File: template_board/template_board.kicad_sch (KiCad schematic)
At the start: 3 parts

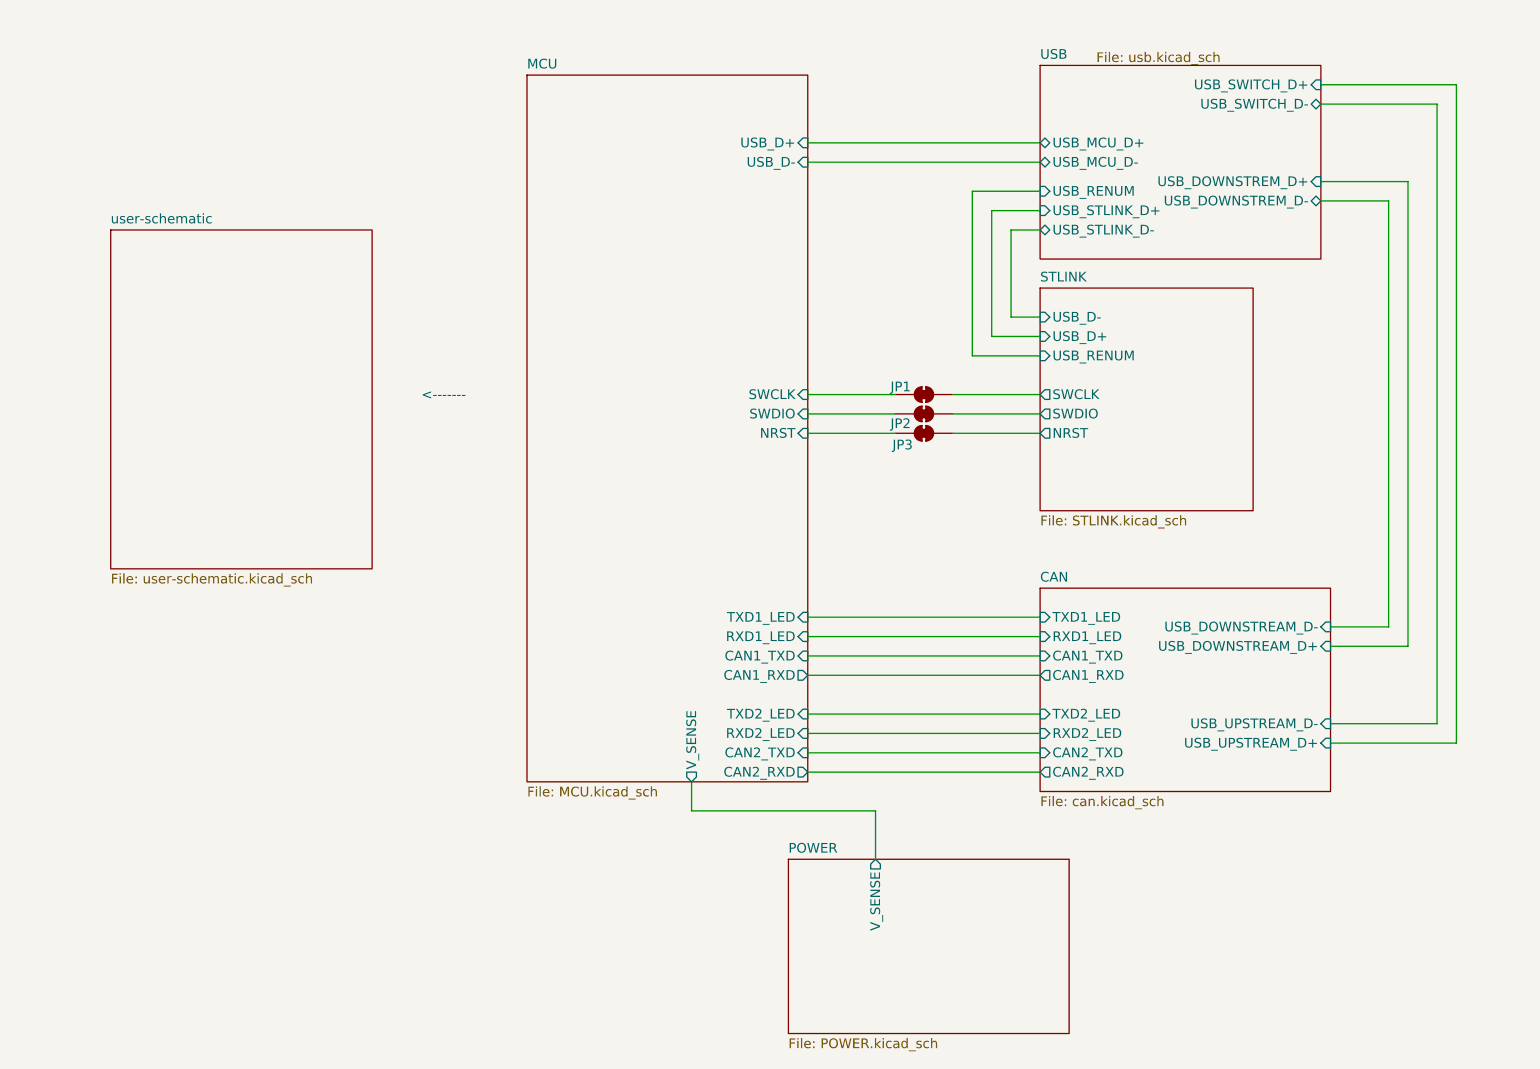
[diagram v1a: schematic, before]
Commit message: updated all subschematics
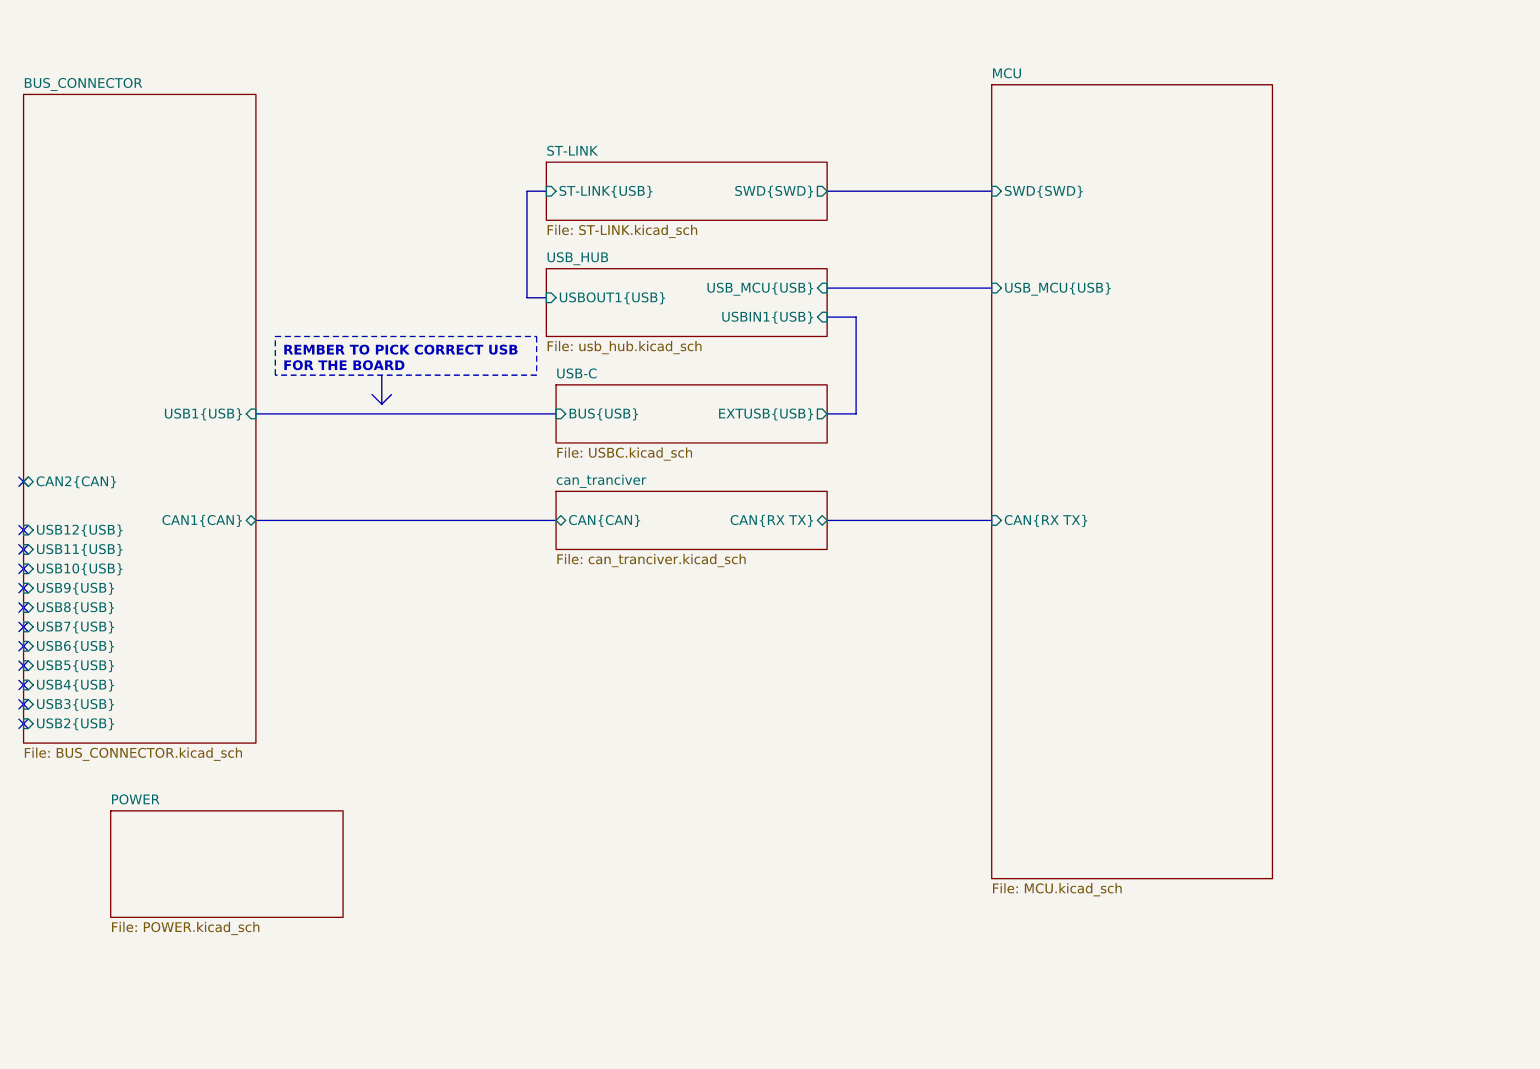
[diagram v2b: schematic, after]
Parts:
- removed JP1, JP2, JP3: SolderJumper_2_Bridged, Jumper:SolderJumper-2_P1.3mm_Open_RoundedPad1.0x1.5mm, symbol Jumper:SolderJumper_2_Bridged
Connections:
- no-connect marks 0 -> 12
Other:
- removed sheet CAN
- removed sheet STLINK
- removed sheet USB
- removed sheet user-schematic
- added sheet BUS_CONNECTOR (BUS_CONNECTOR.kicad_sch)
- added sheet ST-LINK (ST-LINK.kicad_sch)
- added sheet USB-C (USBC.kicad_sch)
- added sheet USB_HUB (usb_hub.kicad_sch)
- added sheet can_tranciver (can_tranciver.kicad_sch)
- sheet MCU ports: added CAN{RX TX}, SWD{SWD}, USB_MCU{USB}; removed CAN1_RXD, CAN1_TXD, CAN2_RXD, CAN2_TXD, NRST, RXD1_LED, RXD2_LED, SWCLK, SWDIO, TXD1_LED, TXD2_LED, USB_D+, USB_D-, V_SENSE
- sheet POWER ports: added none; removed V_SENSE
- note removed: "<-------"

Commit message: can transiver update
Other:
- sheet POWER ports: added POWER_EN; removed none
- sheet can_tranciver ports: added POWER_EN; removed none
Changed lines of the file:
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@@
 		(members "D+" "D-")
 	)
+	(junction
+		(at 57.404 134.62)
+		(diameter 0)
+		(color 0 0 0 0)
+	)
 	(no_connect
 		(at 27.94 92.71)
@@
 		)
 	)
+	(wire
+		(pts
+			(xy 57.404 134.62) (xy 76.2 134.62)
+		)
+		(stroke
+			(width 0)
+			(type default)
+		)
+	)
 	(bus
 		(pts
@@
 		)
 	)
+	(wire
+		(pts
+			(xy 57.15 134.62) (xy 57.404 134.62)
+		)
+		(stroke
+			(width 0)
+			(type default)
+		)
+	)
 	(polyline
 		(pts
@@
 		)
 	)
+	(wire
+		(pts
+			(xy 76.2 134.62) (xy 76.2 95.25)
+		)
+		(stroke
+			(width 0)
+			(type default)
+		)
+	)
 	(bus
 		(pts
 			(xy 58.42 91.44) (xy 97.79 91.44)
+		)
+		(stroke
+			(width 0)
+			(type default)
+		)
+	)
+	(wire
+		(pts
+			(xy 76.2 95.25) (xy 97.79 95.25)
 		)
 		(stroke
@@
 	(sheet
 		(at 97.79 87.63)
-		(size 35.56 7.62)
+		(size 35.56 10.668)
 		(fields_autoplaced yes)
 		(stroke
@@
 		)
 		(property "Sheetfile" "can_tranciver.kicad_sch"
-			(at 97.79 95.8346 0)
+			(at 97.79 98.8826 0)
 			(effects
 				(font
@@
 		(pin "CAN{CAN}" bidirectional
 			(at 97.79 91.44 180)
+			(effects
+				(font
+					(size 1.27 1.27)
+				)
+				(justify left)
+			)
+		)
+		(pin "POWER_EN" output
+			(at 97.79 95.25 180)
 			(effects
 				(font
@@
 	)
 	(sheet
-		(at 39.37 129.54)
+		(at 26.924 130.048)
 		(size 30.48 13.97)
 		(fields_autoplaced yes)
@@
 		)
 		(property "Sheetname" "POWER"
-			(at 39.37 128.8284 0)
+			(at 26.924 129.3364 0)
 			(effects
 				(font
@@
 		)
 		(property "Sheetfile" "POWER.kicad_sch"
-			(at 39.37 144.0946 0)
+			(at 26.924 144.6026 0)
 			(effects
 				(font
@@
 			)
 		)
+		(pin "POWER_EN" input
+			(at 57.404 134.62 0)
+			(effects
+				(font
+					(size 1.27 1.27)
+				)
+				(justify right)
+			)
+		)

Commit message: chamt skończony chyba
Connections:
- no-connect marks 12 -> 15
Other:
- sheet BUS_CONNECTOR ports: added CAN3{CAN}, CAN4{CAN}, GPIO[0..35]; removed none
- sheet MCU ports: added CAN_TRANSIVER{SPI}; removed none
- sheet can_tranciver ports: added CAN_TRANSIVER{SPI}; removed none

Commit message: schemat skończony
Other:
- sheet MCU ports: added STLINK_UART{UART}; removed none
- sheet ST-LINK ports: added STLINK_UART{UART}; removed none
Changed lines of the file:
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@@
+	(bus
+		(pts
+			(xy 166.37 52.07) (xy 187.96 52.07)
+		)
+		(stroke
+			(width 0)
+			(type default)
+		)
+	)
 	(bus
 		(pts
@@
 	(bus
 		(pts
-			(xy 127 53.34) (xy 129.54 53.34)
-		)
-		(stroke
-			(width 0)
-			(type default)
-		)
-	)
-	(bus
-		(pts
-			(xy 166.37 53.34) (xy 187.96 53.34)
+			(xy 127 52.07) (xy 129.54 52.07)
+		)
+		(stroke
+			(width 0)
+			(type default)
+		)
+	)
+	(bus
+		(pts
+			(xy 166.37 49.53) (xy 187.96 49.53)
 		)
 		(stroke
@@
 	(bus
 		(pts
-			(xy 127 67.31) (xy 127 53.34)
+			(xy 127 67.31) (xy 127 52.07)
 		)
 		(stroke
@@
 	(text_box "REMBER \nTO \nPICK \nCORRECT \nUSB \nFOR \nTHE BOARD"
 		(exclude_from_sim no)
-		(at 45.085 95.25 0)
+		(at 45.085 94.615 0)
 		(size 30.48 30.48)
 		(stroke
@@
 			)
 		)
-		(pin "SWD{SWD}" input
-			(at 187.96 53.34 180)
-			(effects
-				(font
-					(size 1.27 1.27)
-				)
-				(justify left)
-			)
-		)
 		(pin "USB_MCU{USB}" input
 			(at 187.96 66.04 180)
@@
 		(pin "CAN_TRANSIVER{SPI}" bidirectional
 			(at 187.96 106.68 180)
+			(effects
+				(font
+					(size 1.27 1.27)
+				)
+				(justify left)
+			)
+		)
+		(pin "STLINK_UART{UART}" bidirectional
+			(at 187.96 52.07 180)
+			(effects
+				(font
+					(size 1.27 1.27)
+				)
+				(justify left)
+			)
+		)
+		(pin "SWD{SWD}" input
+			(at 187.96 49.53 180)
 			(effects
 				(font
@@
 	)
 	(sheet
-		(at 129.54 49.53)
-		(size 36.83 7.62)
+		(at 129.54 46.99)
+		(size 36.83 10.16)
 		(fields_autoplaced yes)
 		(stroke
@@
 		)
 		(property "Sheetname" "ST-LINK"
-			(at 129.54 48.8184 0)
+			(at 129.54 46.2784 0)
 			(effects
 				(font
@@
 			)
 		)
+		(pin "STLINK_UART{UART}" bidirectional
+			(at 166.37 52.07 0)
+			(effects
+				(font
+					(size 1.27 1.27)
+				)
+				(justify right)
+			)
+		)
+		(pin "SWD{SWD}" output
+			(at 166.37 49.53 0)
+			(effects
+				(font
+					(size 1.27 1.27)
+				)
+				(justify right)
+			)
+		)
 		(pin "ST-LINK{USB}" input
-			(at 129.54 53.34 180)
-			(effects
-				(font
-					(size 1.27 1.27)
-				)
-				(justify left)
-			)
-		)
-		(pin "SWD{SWD}" output
-			(at 166.37 53.34 0)
-			(effects
-				(font
-					(size 1.27 1.27)
-				)
-				(justify right)
-			)
-		)
+			(at 129.54 52.07 180)
+			(effects
+				(font
+					(size 1.27 1.27)
+				)
+				(justify left)
+			)
+		)

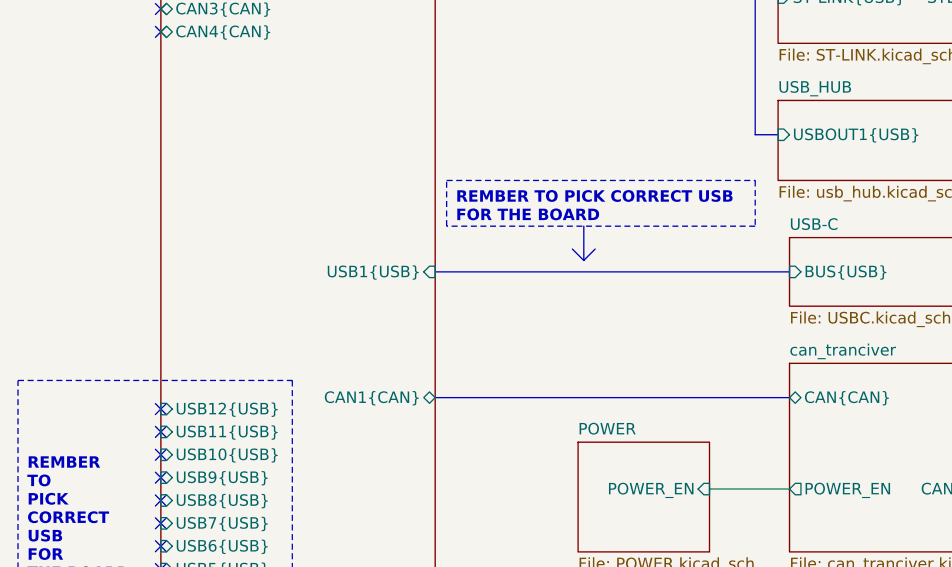
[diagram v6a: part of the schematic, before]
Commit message: [schematics] fixed issue with: stlink->crystal capacitors, usb-> esd with too big capacitance, tranzistor for stlink-usb renum changed
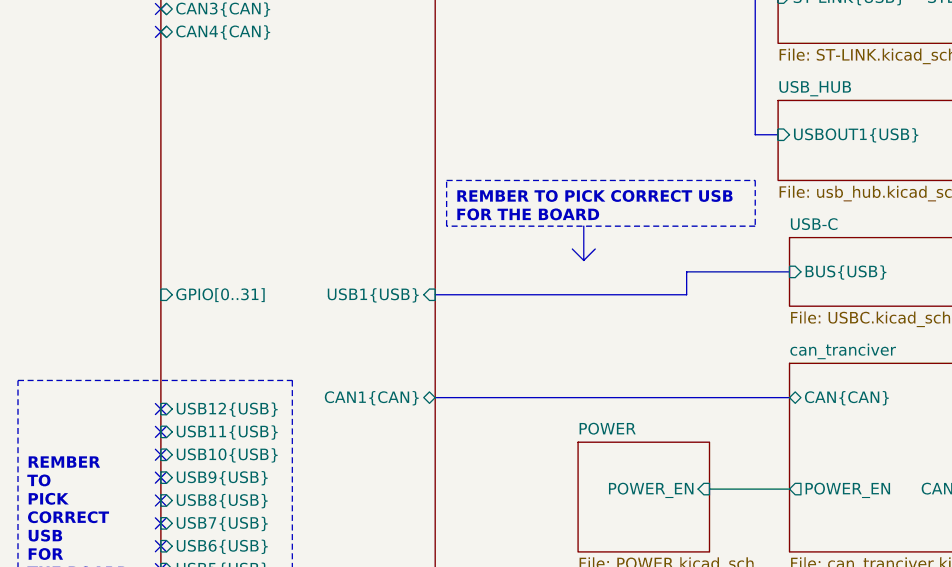
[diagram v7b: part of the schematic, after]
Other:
- sheet BUS_CONNECTOR ports: added GPIO[0..31]; removed none
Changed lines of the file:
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@@
+		)
+	)
+	(bus
+		(pts
+			(xy 119.38 82.55) (xy 130.81 82.55)
+		)
+		(stroke
+			(width 0)
+			(type default)
 		)
 	)
@@
 		)
 	)
+	(bus
+		(pts
+			(xy 91.44 85.09) (xy 119.38 85.09)
+		)
+		(stroke
+			(width 0)
+			(type default)
+		)
+	)
 	(polyline
 		(pts
@@
 	(bus
 		(pts
-			(xy 91.44 82.55) (xy 130.81 82.55)
+			(xy 119.38 85.09) (xy 119.38 82.55)
 		)
 		(stroke
@@
 			)
 		)
-		(pin "USB1{USB}" input
-			(at 91.44 82.55 0)
-			(effects
-				(font
-					(size 1.27 1.27)
-				)
-				(justify right)
-			)
-		)
 		(pin "USB2{USB}" input
 			(at 60.96 123.19 180)
@@
 				)
 				(justify right)
+			)
+		)
+		(pin "USB1{USB}" input
+			(at 91.44 85.09 0)
+			(effects
+				(font
+					(size 1.27 1.27)
+				)
+				(justify right)
+			)
+		)
+		(pin "GPIO[0..31]" input
+			(at 60.96 85.09 180)
+			(effects
+				(font
+					(size 1.27 1.27)
+				)
+				(justify left)
 			)
 		)
@@
 			)
 		)
+		(pin "EXTUSB{USB}" output
+			(at 166.37 82.55 0)
+			(effects
+				(font
+					(size 1.27 1.27)
+				)
+				(justify right)
+			)
+		)
 		(pin "BUS{USB}" input
 			(at 130.81 82.55 180)
@@
 			)
 		)
-		(pin "EXTUSB{USB}" output
-			(at 166.37 82.55 0)
-			(effects
-				(font
-					(size 1.27 1.27)
-				)
-				(justify right)
-			)
-		)

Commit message: [schematics] complete lora board
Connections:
- no-connect marks 15 -> 14
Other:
- added sheet LORA (lora.kicad_sch)
- sheet BUS_CONNECTOR ports: added none; removed GPIO[0..35]
- sheet MCU ports: added GPIO[0..31], LORA_DIO[0..5], LORA{SPI}, ~{LORA_RESET}; removed none
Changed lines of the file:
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@@
 		(at 60.96 50.8)
 	)
-	(no_connect
-		(at 91.44 50.8)
+	(bus
+		(pts
+			(xy 166.37 49.53) (xy 187.96 49.53)
+		)
+		(stroke
+			(width 0)
+			(type default)
+		)
+	)
+	(bus
+		(pts
+			(xy 119.38 82.55) (xy 130.81 82.55)
+		)
+		(stroke
+			(width 0)
+			(type default)
+		)
+	)
+	(polyline
+		(pts
+			(xy 106.68 80.01) (xy 107.95 81.28)
+		)
+		(stroke
+			(width 0)
+			(type default)
+		)
+	)
+	(bus
+		(pts
+			(xy 166.37 33.02) (xy 187.96 33.02)
+		)
+		(stroke
+			(width 0)
+			(type default)
+		)
+	)
+	(wire
+		(pts
+			(xy 121.92 106.68) (xy 130.81 106.68)
+		)
+		(stroke
+			(width 0)
+			(type default)
+		)
+	)
+	(bus
+		(pts
+			(xy 171.45 69.85) (xy 166.37 69.85)
+		)
+		(stroke
+			(width 0)
+			(type default)
+		)
+	)
+	(bus
+		(pts
+			(xy 127 52.07) (xy 129.54 52.07)
+		)
+		(stroke
+			(width 0)
+			(type default)
+		)
+	)
+	(bus
+		(pts
+			(xy 91.44 85.09) (xy 119.38 85.09)
+		)
+		(stroke
+			(width 0)
+			(type default)
+		)
+	)
+	(polyline
+		(pts
+			(xy 107.95 81.28) (xy 109.22 80.01)
+		)
+		(stroke
+			(width 0)
+			(type default)
+		)
+	)
+	(wire
+		(pts
+			(xy 166.37 35.56) (xy 187.96 35.56)
+		)
+		(stroke
+			(width 0)
+			(type default)
+		)
 	)
 	(bus
@@
 	(bus
 		(pts
-			(xy 119.38 82.55) (xy 130.81 82.55)
+			(xy 166.37 66.04) (xy 187.96 66.04)
+		)
+		(stroke
+			(width 0)
+			(type default)
+		)
+	)
+	(bus
+		(pts
+			(xy 166.37 96.52) (xy 187.96 96.52)
 		)
 		(stroke
@@
 	(polyline
 		(pts
-			(xy 106.68 80.01) (xy 107.95 81.28)
-		)
-		(stroke
-			(width 0)
-			(type default)
-		)
-	)
-	(wire
-		(pts
-			(xy 121.92 106.68) (xy 130.81 106.68)
-		)
-		(stroke
-			(width 0)
-			(type default)
-		)
-	)
-	(bus
-		(pts
-			(xy 166.37 66.04) (xy 187.96 66.04)
+			(xy 107.95 77.47) (xy 107.95 81.28)
+		)
+		(stroke
+			(width 0)
+			(type default)
+		)
+	)
+	(bus
+		(pts
+			(xy 166.37 30.48) (xy 187.96 30.48)
+		)
+		(stroke
+			(width 0)
+			(type default)
+		)
+	)
+	(bus
+		(pts
+			(xy 127 67.31) (xy 127 52.07)
+		)
+		(stroke
+			(width 0)
+			(type default)
+		)
+	)
+	(bus
+		(pts
+			(xy 166.37 82.55) (xy 171.45 82.55)
+		)
+		(stroke
+			(width 0)
+			(type default)
+		)
+	)
+	(bus
+		(pts
+			(xy 171.45 82.55) (xy 171.45 69.85)
+		)
+		(stroke
+			(width 0)
+			(type default)
+		)
+	)
+	(bus
+		(pts
+			(xy 91.44 96.52) (xy 130.81 96.52)
 		)
 		(stroke
@@
 	(bus
 		(pts
-			(xy 171.45 69.85) (xy 166.37 69.85)
-		)
-		(stroke
-			(width 0)
-			(type default)
-		)
-	)
-	(bus
-		(pts
-			(xy 127 52.07) (xy 129.54 52.07)
-		)
-		(stroke
-			(width 0)
-			(type default)
-		)
-	)
-	(bus
-		(pts
-			(xy 166.37 49.53) (xy 187.96 49.53)
-		)
-		(stroke
-			(width 0)
-			(type default)
-		)
-	)
-	(bus
-		(pts
-			(xy 91.44 85.09) (xy 119.38 85.09)
-		)
-		(stroke
-			(width 0)
-			(type default)
-		)
-	)
-	(polyline
-		(pts
-			(xy 107.95 81.28) (xy 109.22 80.01)
-		)
-		(stroke
-			(width 0)
-			(type default)
-		)
-	)
-	(polyline
-		(pts
-			(xy 107.95 77.47) (xy 107.95 81.28)
-		)
-		(stroke
-			(width 0)
-			(type default)
-		)
-	)
-	(bus
-		(pts
-			(xy 127 67.31) (xy 127 52.07)
-		)
-		(stroke
-			(width 0)
-			(type default)
-		)
-	)
-	(bus
-		(pts
-			(xy 166.37 82.55) (xy 171.45 82.55)
-		)
-		(stroke
-			(width 0)
-			(type default)
-		)
-	)
-	(bus
-		(pts
-			(xy 171.45 82.55) (xy 171.45 69.85)
-		)
-		(stroke
-			(width 0)
-			(type default)
-		)
-	)
-	(bus
-		(pts
-			(xy 91.44 96.52) (xy 130.81 96.52)
-		)
-		(stroke
-			(width 0)
-			(type default)
-		)
-	)
-	(bus
-		(pts
 			(xy 119.38 85.09) (xy 119.38 82.55)
 		)
@@
 	(bus
 		(pts
-			(xy 166.37 96.52) (xy 187.96 96.52)
+			(xy 91.44 43.18) (xy 187.96 43.18)
 		)
 		(stroke
@@
 			)
 		)
-		(pin "GPIO[0..35]" input
-			(at 91.44 50.8 0)
-			(effects
-				(font
-					(size 1.27 1.27)
-				)
-				(justify right)
-			)
-		)
 		(pin "USB1{USB}" input
 			(at 91.44 85.09 0)
@@
 		)
 		(pin "GPIO[0..31]" input
-			(at 60.96 85.09 180)
-			(effects
-				(font
-					(size 1.27 1.27)
-				)
-				(justify left)
+			(at 91.44 43.18 0)
+			(effects
+				(font
+					(size 1.27 1.27)
+				)
+				(justify right)
 			)
 		)
@@
 	)
 	(sheet
-		(at 187.96 39.37)
+		(at 187.96 27.94)
 		(size 36.83 104.14)
 		(fields_autoplaced yes)
@@
 		)
 		(property "Sheetname" "MCU"
-			(at 187.96 38.6584 0)
+			(at 187.96 27.2284 0)
 			(effects
 				(font
@@
 		)
 		(property "Sheetfile" "MCU.kicad_sch"
-			(at 187.96 144.0946 0)
+			(at 187.96 132.6646 0)
 			(effects
 				(font
@@
 		(pin "SWD{SWD}" input
 			(at 187.96 49.53 180)
+			(effects
+				(font
+					(size 1.27 1.27)
+				)
+				(justify left)
+			)
+		)
+		(pin "LORA_DIO[0..5]" bidirectional
+			(at 187.96 30.48 180)
+			(effects
+				(font
+					(size 1.27 1.27)
+				)
+				(justify left)
+			)
+		)
+		(pin "~{LORA_RESET}" input
+			(at 187.96 35.56 180)
+			(effects
+				(font
+					(size 1.27 1.27)
+				)
+				(justify left)
+			)
+		)
+		(pin "LORA{SPI}" bidirectional
+			(at 187.96 33.02 180)
+			(effects
+				(font
+					(size 1.27 1.27)
+				)
+				(justify left)
+			)
+		)
+		(pin "GPIO[0..31]" input
+			(at 187.96 43.18 180)
 			(effects
 				(font
@@
 				)
 			)
+		)
+	)
+	(sheet
+		(at 129.54 27.94)
+		(size 36.83 11.43)
+		(fields_autoplaced yes)
+		(stroke
+			(width 0.1524)
+			(type solid)
+		)
+		(fill
+			(color 0 0 0 0.0000)
+		)
+		(property "Sheetname" "LORA"
+			(at 129.54 27.2284 0)
+			(effects
+				(font
+					(size 1.27 1.27)
+				)
+				(justify left bottom)
+			)
+		)
+		(property "Sheetfile" "lora.kicad_sch"
+			(at 129.54 39.9546 0)
+			(effects
+				(font
+					(size 1.27 1.27)
+				)
+				(justify left top)
+			)
+		)
+		(pin "LORA_DIO[0..5]" bidirectional
+			(at 166.37 30.48 0)
+			(effects
+				(font
+					(size 1.27 1.27)
+				)
+				(justify right)
+			)
+		)
+		(pin "~{LORA_RESET}" input
+			(at 166.37 35.56 0)
+			(effects
+				(font
+					(size 1.27 1.27)
+				)
+				(justify right)
+			)
+		)
+		(pin "LORA{SPI}" bidirectional
+			(at 166.37 33.02 0)
+			(effects
+				(font
+					(size 1.27 1.27)
+				)
+				(justify right)
+			)
+		)
+		(instances
+			(project "template_board"
+				(path "/f131027f-631c-4099-b0ec-5f883860005f"
+					(page "9")
+				)
+			)
